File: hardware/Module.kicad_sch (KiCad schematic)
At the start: 119 parts, among them J1 Jack, J10 Jack, J11 Jack, J12 Jack, J13 Micro_SD, J14 NW_B, J15 Jack, J16 Jack, J17 Power, J18 Jack, J19 Jack, J2 OLED, J20 SW_B, J21 NW_A, J22 SW_A, J23 NE_A, J3 NE_B, J4 Jack, J5 Jack, J6 Jack, J7 Jack, J8 Jack, J9 Jack, SW1 Encoder, U1 TL074, U2 TL074, U3 TL074, U4 MCP6004, U5 MCP6002, U7 LM4040C10

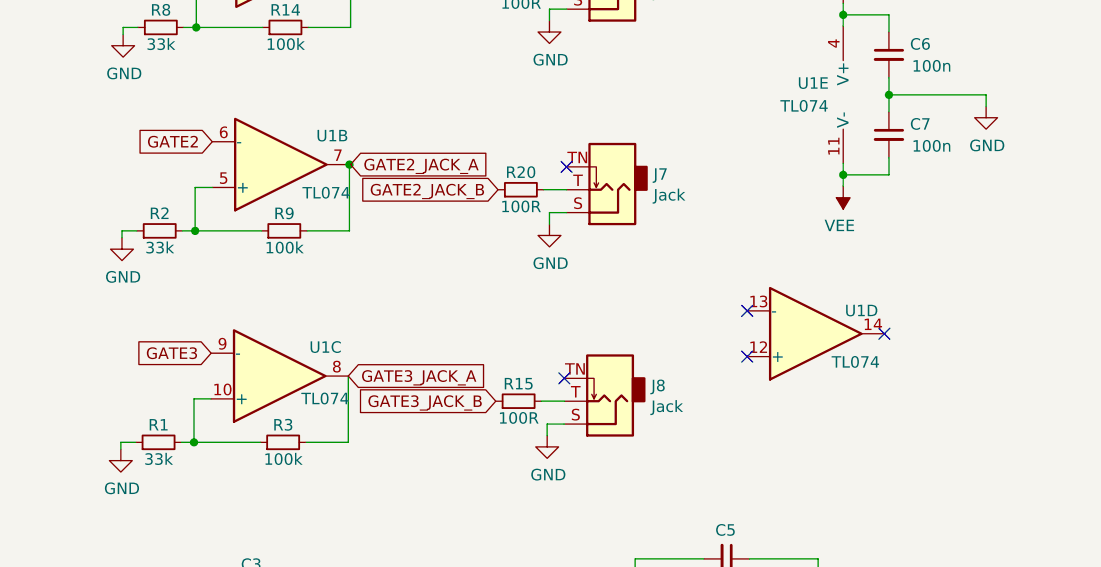
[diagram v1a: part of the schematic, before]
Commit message: Test gate outputs and document its bugs
Signed-off-by: Petr Horacek <hrck@protonmail.com>
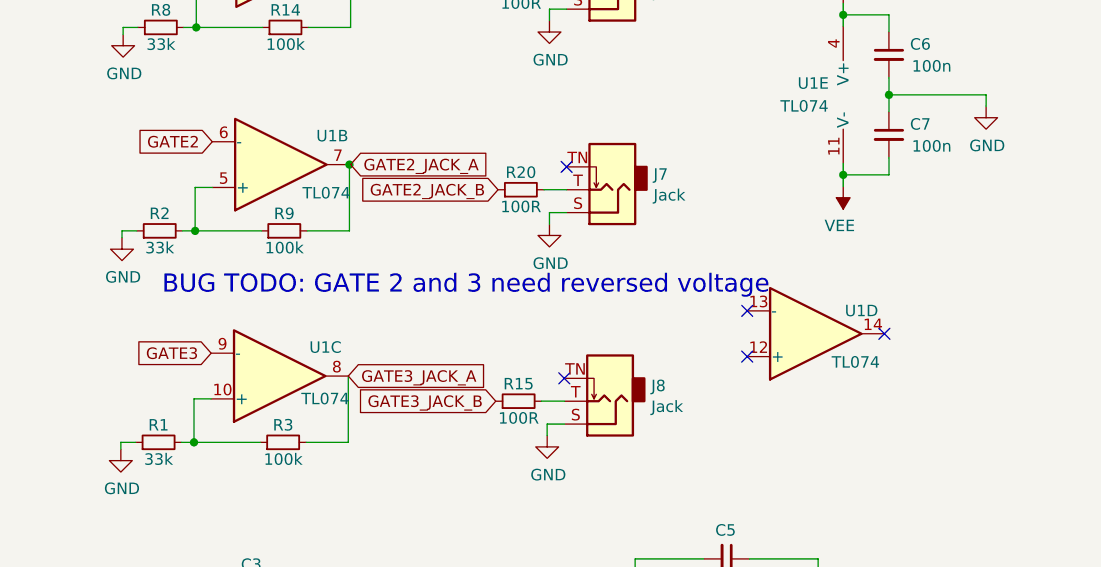
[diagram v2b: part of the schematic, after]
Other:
- note added: "BUG TODO: GATE 2 and 3 need reversed voltage"
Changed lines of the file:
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@@
     (effects (font (size 1.27 1.27)) (justify left bottom))
+  )
+  (text "BUG TODO: GATE 2 and 3 need reversed voltage" (at 146.812 187.071 0)
+    (effects (font (size 2.0066 2.0066)) (justify left bottom))
   )
   (text "CS" (at 63.373 254.635 0)
